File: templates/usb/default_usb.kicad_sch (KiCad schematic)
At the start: 4 parts

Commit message: update footprint lib to ergocai.pretty
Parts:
- USB_J1: footprint ErgoCai:USB_C_Receptacle_HRO_TYPE-C-31-M-12 -> ErgoCai.pretty:USB_C_Receptacle_HRO_TYPE-C-31-M-12
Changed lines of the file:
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@@
 		(pin "2"
-		)
-		(instances
-			(project "ergo_cai"
-				(path "/4ad52d44-7e09-4b14-9ca9-1745a5702ae6/aa2d854c-6250-43f0-93ec-e020981ba8ea"
-					(reference "USB_R_CC2")
-					(unit 1)
-				)
-			)
 		)
 	)
@@
 			)
 		)
-		(property "Footprint" "ErgoCai:USB_C_Receptacle_HRO_TYPE-C-31-M-12"
+		(property "Footprint" "ErgoCai.pretty:USB_C_Receptacle_HRO_TYPE-C-31-M-12"
 			(at 93.98 85.09 0)
 			(effects
@@
 		)
 		(instances
-			(project "ergo_cai"
-				(path "/4ad52d44-7e09-4b14-9ca9-1745a5702ae6/aa2d854c-6250-43f0-93ec-e020981ba8ea"
+			(project ""
+				(path "/4ad52d44-7e09-4b14-9ca9-1745a5702ae6/8c853b1d-d586-4380-a2bc-921f5653e681"
 					(reference "USB_J1")
 					(unit 1)
@@
 		)
 		(instances
-			(project "ergo_cai"
-				(path "/4ad52d44-7e09-4b14-9ca9-1745a5702ae6/aa2d854c-6250-43f0-93ec-e020981ba8ea"
+			(project ""
+				(path "/4ad52d44-7e09-4b14-9ca9-1745a5702ae6/8c853b1d-d586-4380-a2bc-921f5653e681"
 					(reference "#PWR01")
 					(unit 1)
@@
 		)
 		(instances
-			(project "ergo_cai"
-				(path "/4ad52d44-7e09-4b14-9ca9-1745a5702ae6/aa2d854c-6250-43f0-93ec-e020981ba8ea"
+			(project ""
+				(path "/4ad52d44-7e09-4b14-9ca9-1745a5702ae6/8c853b1d-d586-4380-a2bc-921f5653e681"
 					(reference "#PWR03")
 					(unit 1)
@@
 		)
 		(instances
-			(project "ergo_cai"
-				(path "/4ad52d44-7e09-4b14-9ca9-1745a5702ae6/aa2d854c-6250-43f0-93ec-e020981ba8ea"
+			(project ""
+				(path "/4ad52d44-7e09-4b14-9ca9-1745a5702ae6/8c853b1d-d586-4380-a2bc-921f5653e681"
 					(reference "#PWR02")
 					(unit 1)
@@
 		(pin "2"
 		)
-		(instances
-			(project "ergo_cai"
-				(path "/4ad52d44-7e09-4b14-9ca9-1745a5702ae6/aa2d854c-6250-43f0-93ec-e020981ba8ea"
-					(reference "USB_C1")
-					(unit 1)
-				)
-			)
-		)
 	)
 	(symbol
@@
 		)
 		(instances
-			(project "ergo_cai"
-				(path "/4ad52d44-7e09-4b14-9ca9-1745a5702ae6/aa2d854c-6250-43f0-93ec-e020981ba8ea"
+			(project ""
+				(path "/4ad52d44-7e09-4b14-9ca9-1745a5702ae6/8c853b1d-d586-4380-a2bc-921f5653e681"
 					(reference "#PWR07")
 					(unit 1)
@@
 		(pin "2"
 		)
-		(instances
-			(project "ergo_cai"
-				(path "/4ad52d44-7e09-4b14-9ca9-1745a5702ae6/aa2d854c-6250-43f0-93ec-e020981ba8ea"
-					(reference "USB_R_CC1")
-					(unit 1)
-				)
-			)
-		)
-	)
+	)

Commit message: update sch files
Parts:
- USB_R_CC1, USB_R_CC2: footprint ErgoCai:R_0603 -> ErgoCai.pretty:R_0603_1608Metric
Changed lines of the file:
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@@
 			)
 		)
-		(property "Footprint" "ErgoCai:R_0603"
+		(property "Footprint" "ErgoCai.pretty:R_0603_1608Metric"
 			(at 123.19 109.22 0)
 			(effects
@@
 			)
 		)
-		(property "Description" ""
+		(property "Description" "Resistor, small symbol"
 			(at 123.19 109.22 0)
 			(effects
@@
 		(instances
 			(project ""
-				(path "/4ad52d44-7e09-4b14-9ca9-1745a5702ae6/8c853b1d-d586-4380-a2bc-921f5653e681"
+				(path "/4ad52d44-7e09-4b14-9ca9-1745a5702ae6/eab2ad23-b528-4672-a6fc-854157c306db"
 					(reference "USB_J1")
 					(unit 1)
@@
 			)
 		)
-		(property "Description" ""
+		(property "Description" "Power symbol creates a global label with name \"GND\" , ground"
 			(at 90.17 109.22 0)
 			(effects
@@
 		(instances
 			(project ""
-				(path "/4ad52d44-7e09-4b14-9ca9-1745a5702ae6/8c853b1d-d586-4380-a2bc-921f5653e681"
+				(path "/4ad52d44-7e09-4b14-9ca9-1745a5702ae6/eab2ad23-b528-4672-a6fc-854157c306db"
 					(reference "#PWR01")
 					(unit 1)
@@
 			)
 		)
-		(property "Description" ""
+		(property "Description" "Power symbol creates a global label with name \"GND\" , ground"
 			(at 123.19 111.76 0)
 			(effects
@@
 		(instances
 			(project ""
-				(path "/4ad52d44-7e09-4b14-9ca9-1745a5702ae6/8c853b1d-d586-4380-a2bc-921f5653e681"
+				(path "/4ad52d44-7e09-4b14-9ca9-1745a5702ae6/eab2ad23-b528-4672-a6fc-854157c306db"
 					(reference "#PWR03")
 					(unit 1)
@@
 			)
 		)
-		(property "Description" ""
+		(property "Description" "Power symbol creates a global label with name \"GND\" , ground"
 			(at 105.41 111.76 0)
 			(effects
@@
 		(instances
 			(project ""
-				(path "/4ad52d44-7e09-4b14-9ca9-1745a5702ae6/8c853b1d-d586-4380-a2bc-921f5653e681"
+				(path "/4ad52d44-7e09-4b14-9ca9-1745a5702ae6/eab2ad23-b528-4672-a6fc-854157c306db"
 					(reference "#PWR02")
 					(unit 1)
@@
 			)
 		)
-		(property "Description" ""
+		(property "Description" "Unpolarized capacitor"
 			(at 142.24 111.76 0)
 			(effects
@@
 			)
 		)
-		(property "Description" ""
+		(property "Description" "Power symbol creates a global label with name \"GND\" , ground"
 			(at 142.24 115.57 0)
 			(effects
@@
 		(instances
 			(project ""
-				(path "/4ad52d44-7e09-4b14-9ca9-1745a5702ae6/8c853b1d-d586-4380-a2bc-921f5653e681"
+				(path "/4ad52d44-7e09-4b14-9ca9-1745a5702ae6/eab2ad23-b528-4672-a6fc-854157c306db"
 					(reference "#PWR07")
 					(unit 1)
@@
 			)
 		)
-		(property "Footprint" "ErgoCai:R_0603"
+		(property "Footprint" "ErgoCai.pretty:R_0603_1608Metric"
 			(at 105.41 109.22 0)
 			(effects
@@
 			)
 		)
-		(property "Description" ""
+		(property "Description" "Resistor, small symbol"
 			(at 105.41 109.22 0)
 			(effects

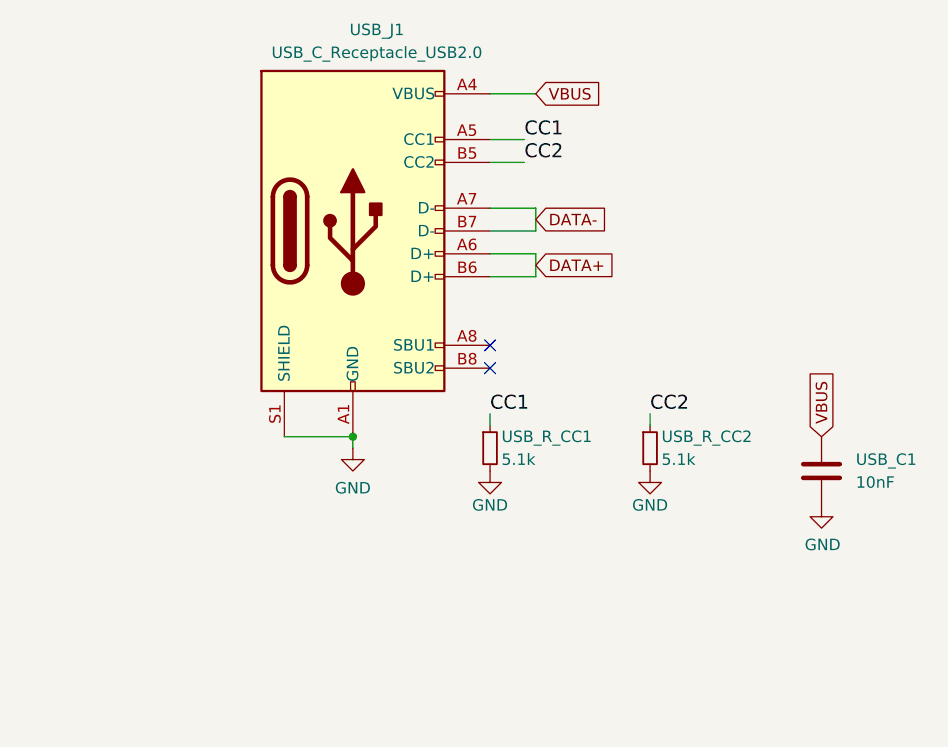
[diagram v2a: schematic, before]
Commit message: correct footprint path, add .pretty update templates
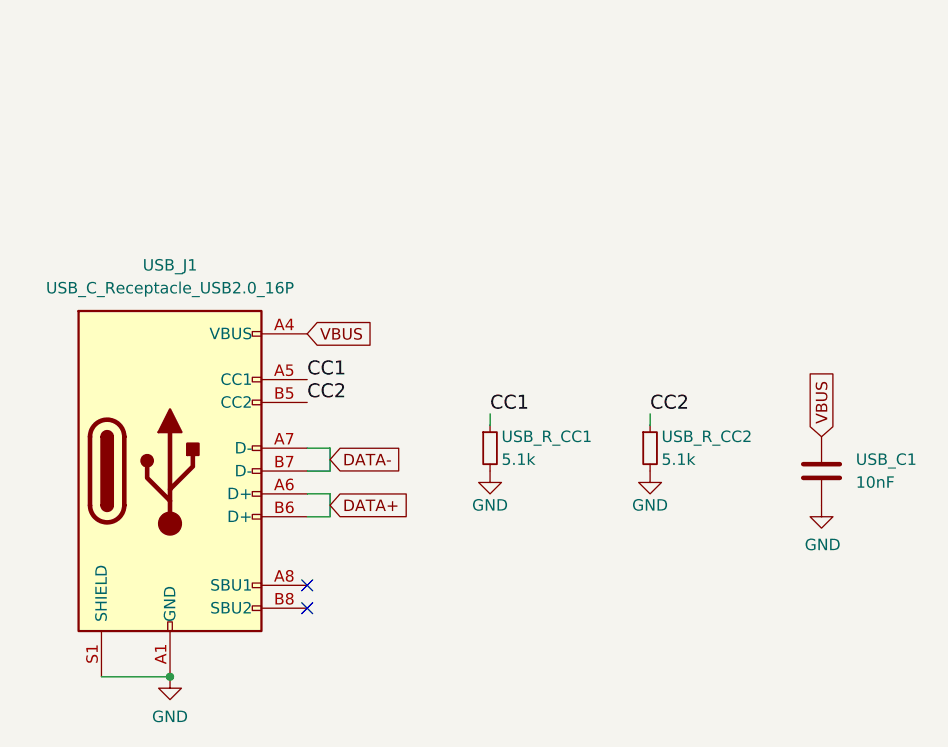
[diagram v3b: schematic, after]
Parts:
- removed USB_J1: USB_C_Receptacle_USB2.0, ErgoCai.pretty:USB_C_Receptacle_HRO_TYPE-C-31-M-12, symbol Connector:USB_C_Receptacle_USB2.0
- added USB_J1: USB_C_Receptacle_USB2.0_16P, ErgoCai.pretty:USB_C_Receptacle_HRO_TYPE-C-31-M-12, symbol Connector:USB_C_Receptacle_USB2.0_16P
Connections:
- net CC1: now also USB_J1.A5 (CC1)
- net CC2: now also USB_J1.B5 (CC2)
- net DATA+: now also USB_J1.A6 (D+), USB_J1.B6 (D+)
- net DATA-: now also USB_J1.A7 (D-), USB_J1.B7 (D-)
- net GND: now also USB_J1.A1 (GND), USB_J1.A12 (GND), USB_J1.B1 (GND), USB_J1.B12 (GND), USB_J1.S1 (SHIELD)
- net VBUS: now also USB_J1.A4 (VBUS), USB_J1.A9 (VBUS), USB_J1.B4 (VBUS), USB_J1.B9 (VBUS)
